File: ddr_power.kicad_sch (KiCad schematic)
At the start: 27 parts, among them U2 MT53D512M32D2DS

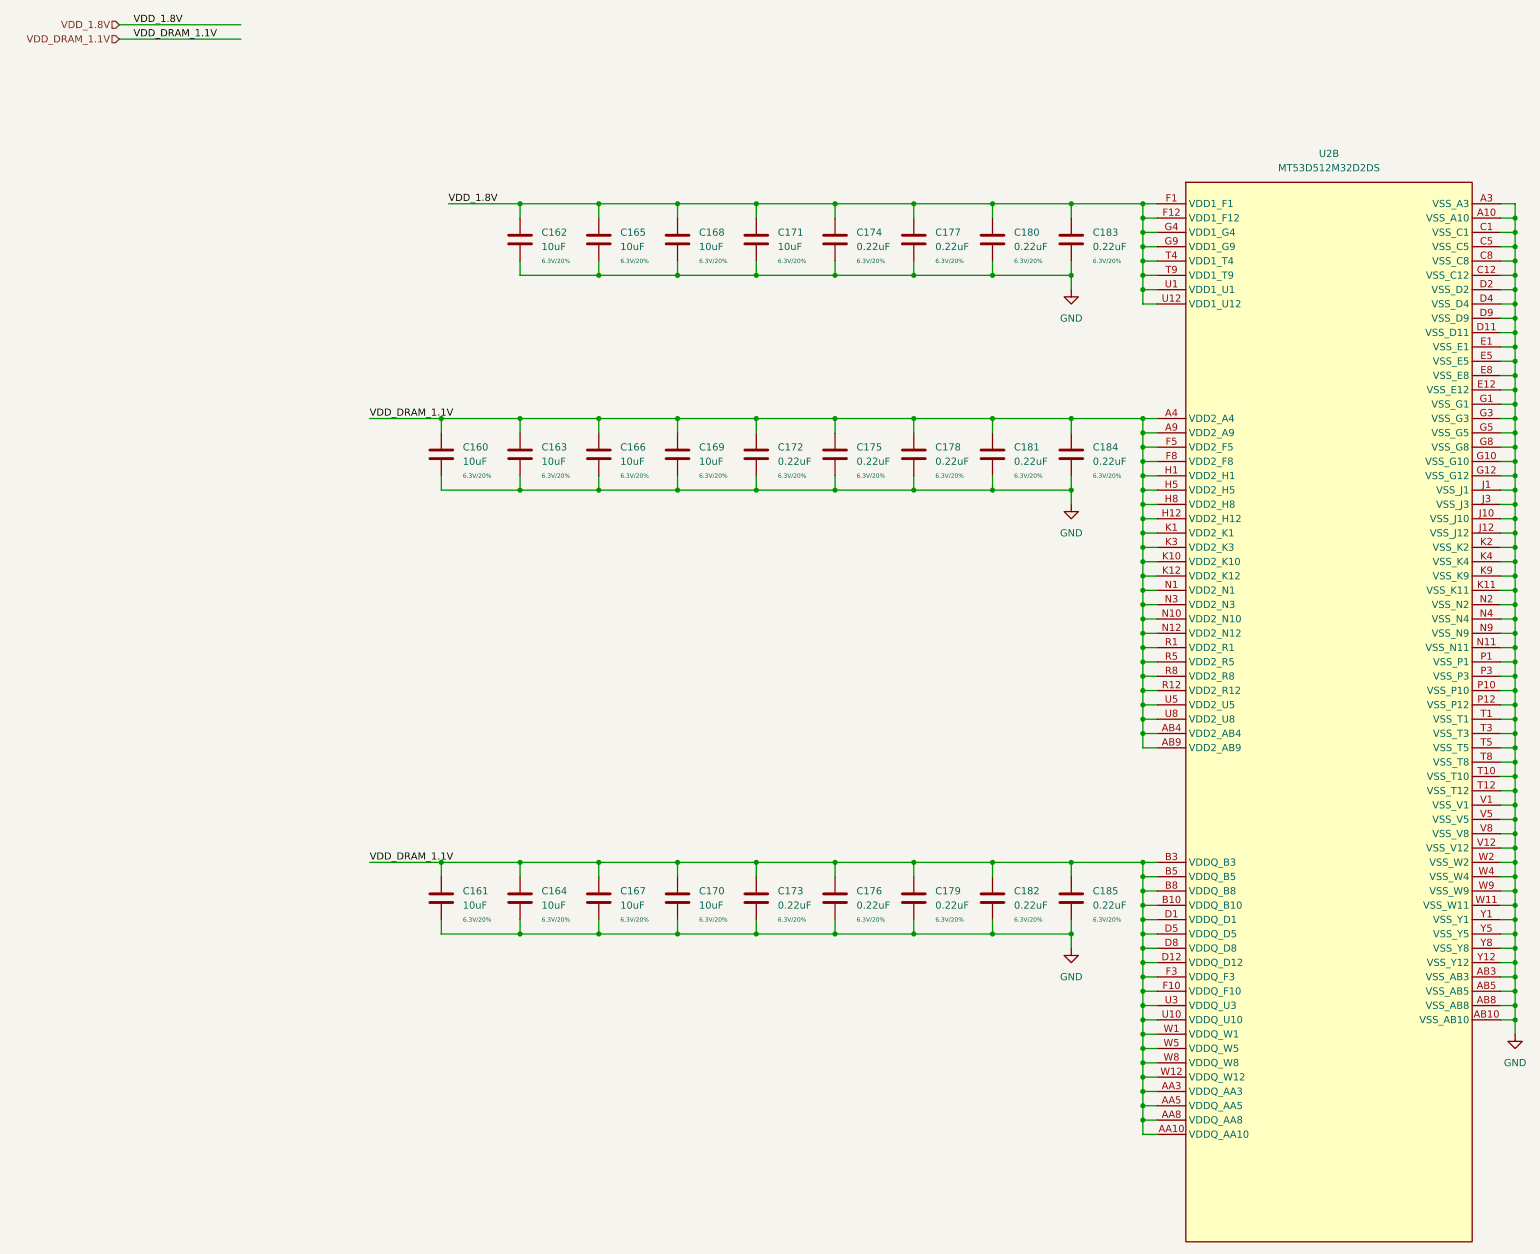
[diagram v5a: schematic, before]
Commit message: misc cleanup, change from usb mux to dual uart
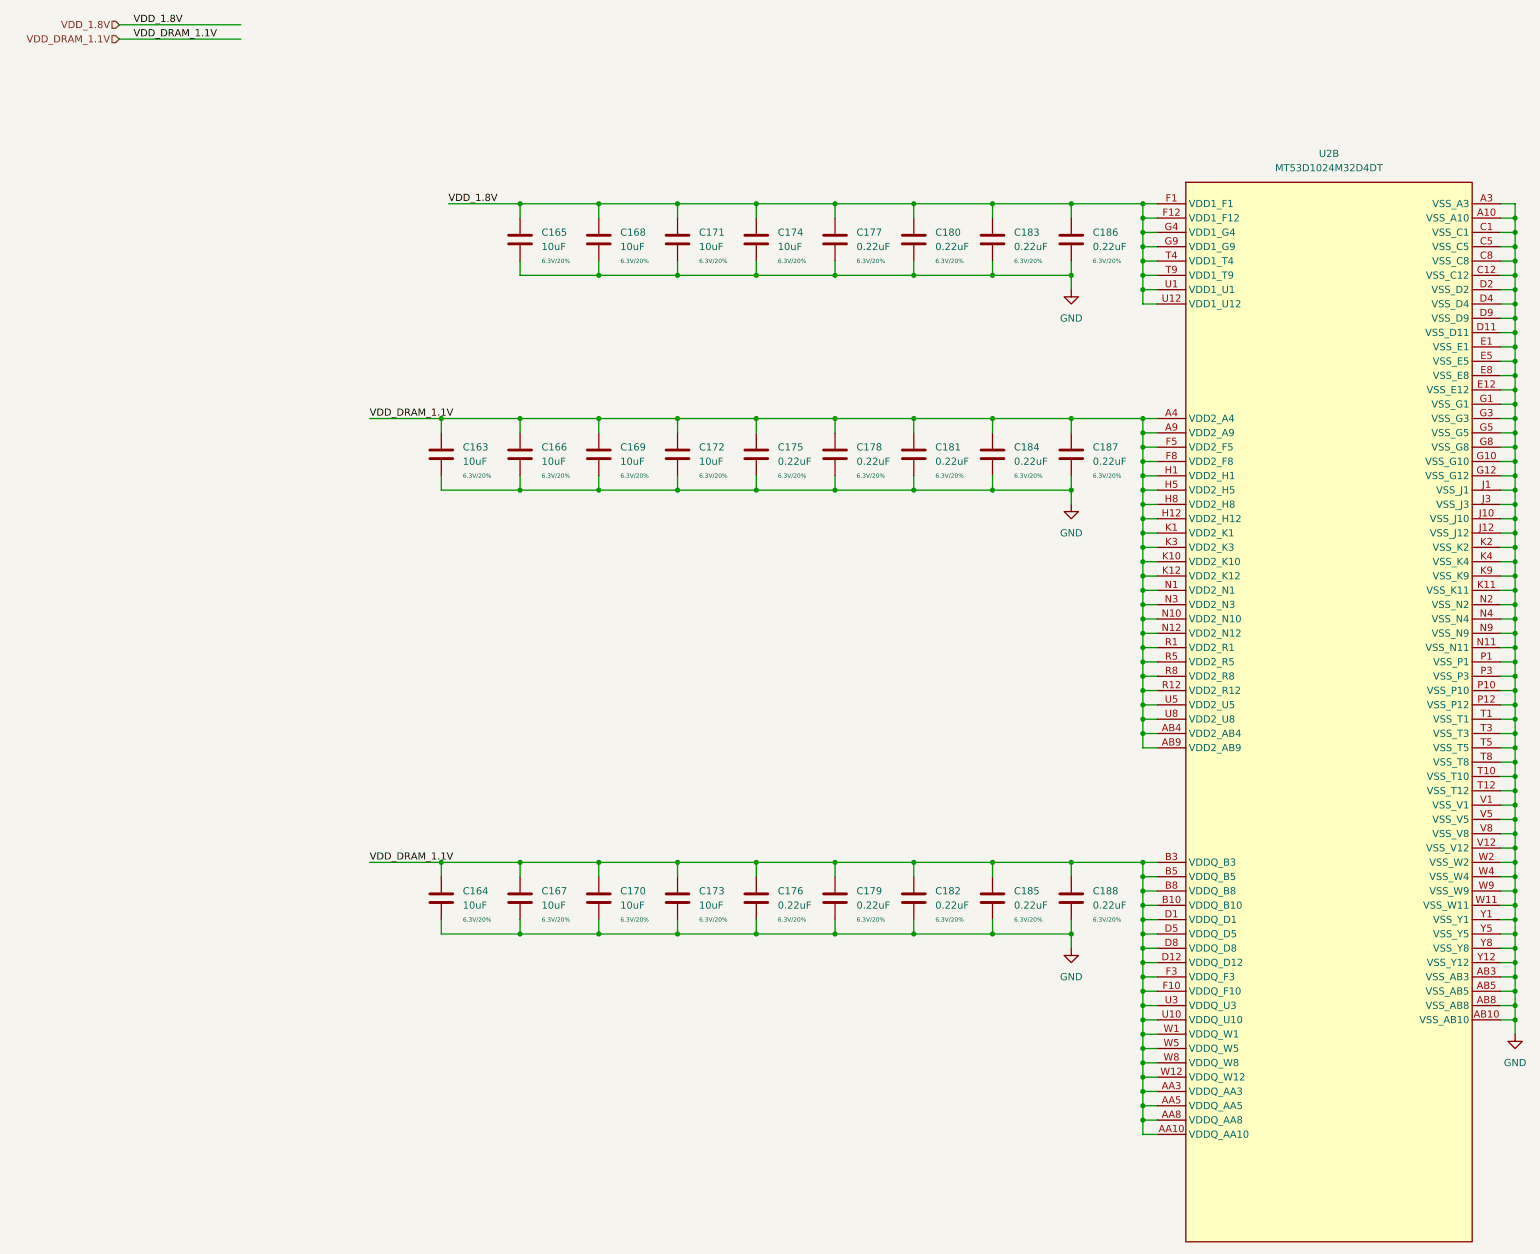
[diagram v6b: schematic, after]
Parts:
- U2: value MT53D512M32D2DS -> MT53D1024M32D4DT
- renumbered C160 to C163, C161 to C164, C162 to C165, C163 to C166, C164 to C167, C165 to C168, C166 to C169, C167 to C170, C168 to C171, C169 to C172, C170 to C173, C171 to C174, C172 to C175, C173 to C176, C174 to C177, C175 to C178, C176 to C179, C177 to C180, C178 to C181, C179 to C182, C180 to C183, C181 to C184, C182 to C185, C183 to C186, C184 to C187, C185 to C188
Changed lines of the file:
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@@
   (symbol (lib_id "Device:C") (at 120.65 59.69 0) (unit 1)
     (in_bom yes) (on_board yes)
-    (property "Reference" "C165" (id 0) (at 124.46 58.4199 0)
+    (property "Reference" "C168" (id 0) (at 124.46 58.4199 0)
       (effects (font (size 1.27 1.27)) (justify left))
     )
@@
   (symbol (lib_id "Device:C") (at 190.5 59.69 0) (unit 1)
     (in_bom yes) (on_board yes)
-    (property "Reference" "C180" (id 0) (at 194.31 58.4199 0)
+    (property "Reference" "C183" (id 0) (at 194.31 58.4199 0)
       (effects (font (size 1.27 1.27)) (justify left))
     )
@@
   (symbol (lib_id "Device:C") (at 162.56 97.79 0) (unit 1)
     (in_bom yes) (on_board yes)
-    (property "Reference" "C175" (id 0) (at 166.37 96.5199 0)
+    (property "Reference" "C178" (id 0) (at 166.37 96.5199 0)
       (effects (font (size 1.27 1.27)) (justify left))
     )
@@
   (symbol (lib_id "Device:C") (at 190.5 176.53 0) (unit 1)
     (in_bom yes) (on_board yes)
-    (property "Reference" "C182" (id 0) (at 194.31 175.2599 0)
+    (property "Reference" "C185" (id 0) (at 194.31 175.2599 0)
       (effects (font (size 1.27 1.27)) (justify left))
     )
@@
     (in_bom yes) (on_board yes) (fields_autoplaced)
     (property "Reference" "U2" (id 0) (at 250.19 44.45 0))
-    (property "Value" "MT53D512M32D2DS" (id 1) (at 250.19 46.99 0))
+    (property "Value" "MT53D1024M32D4DT" (id 1) (at 250.19 46.99 0))
     (property "Footprint" "Package_BGA:BGA-200_10.0x14.5mm_Layout12x22_P0.80x0.65mm" (id 2) (at 250.19 243.84 0)
       (effects (font (size 1.27 1.27)) hide)
@@
   (symbol (lib_id "Device:C") (at 148.59 59.69 0) (unit 1)
     (in_bom yes) (on_board yes)
-    (property "Reference" "C171" (id 0) (at 152.4 58.4199 0)
+    (property "Reference" "C174" (id 0) (at 152.4 58.4199 0)
       (effects (font (size 1.27 1.27)) (justify left))
     )
@@
   (symbol (lib_id "Device:C") (at 190.5 97.79 0) (unit 1)
     (in_bom yes) (on_board yes)
-    (property "Reference" "C181" (id 0) (at 194.31 96.5199 0)
+    (property "Reference" "C184" (id 0) (at 194.31 96.5199 0)
       (effects (font (size 1.27 1.27)) (justify left))
     )
@@
   (symbol (lib_id "Device:C") (at 176.53 59.69 0) (unit 1)
     (in_bom yes) (on_board yes)
-    (property "Reference" "C177" (id 0) (at 180.34 58.4199 0)
+    (property "Reference" "C180" (id 0) (at 180.34 58.4199 0)
       (effects (font (size 1.27 1.27)) (justify left))
     )
@@
   (symbol (lib_id "power:GND") (at 204.47 68.58 0) (unit 1)
     (in_bom yes) (on_board yes) (fields_autoplaced)
-    (property "Reference" "#PWR0156" (id 0) (at 204.47 74.93 0)
+    (property "Reference" "#PWR0160" (id 0) (at 204.47 74.93 0)
       (effects (font (size 1.27 1.27)) hide)
     )
@@
   (symbol (lib_id "Device:C") (at 134.62 59.69 0) (unit 1)
     (in_bom yes) (on_board yes)
-    (property "Reference" "C168" (id 0) (at 138.43 58.4199 0)
+    (property "Reference" "C171" (id 0) (at 138.43 58.4199 0)
       (effects (font (size 1.27 1.27)) (justify left))
     )
@@
   (symbol (lib_id "Device:C") (at 204.47 176.53 0) (unit 1)
     (in_bom yes) (on_board yes)
-    (property "Reference" "C185" (id 0) (at 208.28 175.2599 0)
+    (property "Reference" "C188" (id 0) (at 208.28 175.2599 0)
       (effects (font (size 1.27 1.27)) (justify left))
     )
@@
   (symbol (lib_id "Device:C") (at 92.71 176.53 0) (unit 1)
     (in_bom yes) (on_board yes)
-    (property "Reference" "C161" (id 0) (at 96.52 175.2599 0)
+    (property "Reference" "C164" (id 0) (at 96.52 175.2599 0)
       (effects (font (size 1.27 1.27)) (justify left))
     )
@@
   (symbol (lib_id "Device:C") (at 204.47 97.79 0) (unit 1)
     (in_bom yes) (on_board yes)
-    (property "Reference" "C184" (id 0) (at 208.28 96.5199 0)
+    (property "Reference" "C187" (id 0) (at 208.28 96.5199 0)
       (effects (font (size 1.27 1.27)) (justify left))
     )
@@
   (symbol (lib_id "Device:C") (at 204.47 59.69 0) (unit 1)
     (in_bom yes) (on_board yes)
-    (property "Reference" "C183" (id 0) (at 208.28 58.4199 0)
+    (property "Reference" "C186" (id 0) (at 208.28 58.4199 0)
       (effects (font (size 1.27 1.27)) (justify left))
     )
@@
   (symbol (lib_id "Device:C") (at 120.65 97.79 0) (unit 1)
     (in_bom yes) (on_board yes)
-    (property "Reference" "C166" (id 0) (at 124.46 96.5199 0)
+    (property "Reference" "C169" (id 0) (at 124.46 96.5199 0)
       (effects (font (size 1.27 1.27)) (justify left))
     )
@@
   (symbol (lib_id "Device:C") (at 176.53 176.53 0) (unit 1)
     (in_bom yes) (on_board yes)
-    (property "Reference" "C179" (id 0) (at 180.34 175.2599 0)
+    (property "Reference" "C182" (id 0) (at 180.34 175.2599 0)
       (effects (font (size 1.27 1.27)) (justify left))
     )
@@
   (symbol (lib_id "power:GND") (at 204.47 106.68 0) (unit 1)
     (in_bom yes) (on_board yes) (fields_autoplaced)
-    (property "Reference" "#PWR0157" (id 0) (at 204.47 113.03 0)
+    (property "Reference" "#PWR0161" (id 0) (at 204.47 113.03 0)
       (effects (font (size 1.27 1.27)) hide)
     )
@@
   (symbol (lib_id "power:GND") (at 204.47 185.42 0) (unit 1)
     (in_bom yes) (on_board yes) (fields_autoplaced)
-    (property "Reference" "#PWR0158" (id 0) (at 204.47 191.77 0)
+    (property "Reference" "#PWR0162" (id 0) (at 204.47 191.77 0)
       (effects (font (size 1.27 1.27)) hide)
     )
@@
   (symbol (lib_id "Device:C") (at 162.56 59.69 0) (unit 1)
     (in_bom yes) (on_board yes)
-    (property "Reference" "C174" (id 0) (at 166.37 58.4199 0)
+    (property "Reference" "C177" (id 0) (at 166.37 58.4199 0)
       (effects (font (size 1.27 1.27)) (justify left))
     )
@@
   (symbol (lib_id "Device:C") (at 148.59 97.79 0) (unit 1)
     (in_bom yes) (on_board yes)
-    (property "Reference" "C172" (id 0) (at 152.4 96.5199 0)
+    (property "Reference" "C175" (id 0) (at 152.4 96.5199 0)
       (effects (font (size 1.27 1.27)) (justify left))
     )
@@
   (symbol (lib_id "Device:C") (at 106.68 59.69 0) (unit 1)
     (in_bom yes) (on_board yes)
-    (property "Reference" "C162" (id 0) (at 110.49 58.4199 0)
+    (property "Reference" "C165" (id 0) (at 110.49 58.4199 0)
       (effects (font (size 1.27 1.27)) (justify left))
     )
@@
   (symbol (lib_id "power:GND") (at 283.21 200.66 0) (unit 1)
     (in_bom yes) (on_board yes) (fields_autoplaced)
-    (property "Reference" "#PWR0159" (id 0) (at 283.21 207.01 0)
+    (property "Reference" "#PWR0163" (id 0) (at 283.21 207.01 0)
       (effects (font (size 1.27 1.27)) hide)
     )
@@
   (symbol (lib_id "Device:C") (at 106.68 176.53 0) (unit 1)
     (in_bom yes) (on_board yes)
-    (property "Reference" "C164" (id 0) (at 110.49 175.2599 0)
+    (property "Reference" "C167" (id 0) (at 110.49 175.2599 0)
       (effects (font (size 1.27 1.27)) (justify left))
     )
@@
   (symbol (lib_id "Device:C") (at 134.62 176.53 0) (unit 1)
     (in_bom yes) (on_board yes)
-    (property "Reference" "C170" (id 0) (at 138.43 175.2599 0)
+    (property "Reference" "C173" (id 0) (at 138.43 175.2599 0)
       (effects (font (size 1.27 1.27)) (justify left))
     )
@@
   (symbol (lib_id "Device:C") (at 148.59 176.53 0) (unit 1)
     (in_bom yes) (on_board yes)
-    (property "Reference" "C173" (id 0) (at 152.4 175.2599 0)
+    (property "Reference" "C176" (id 0) (at 152.4 175.2599 0)
       (effects (font (size 1.27 1.27)) (justify left))
     )
@@
   (symbol (lib_id "Device:C") (at 134.62 97.79 0) (unit 1)
     (in_bom yes) (on_board yes)
-    (property "Reference" "C169" (id 0) (at 138.43 96.5199 0)
+    (property "Reference" "C172" (id 0) (at 138.43 96.5199 0)
       (effects (font (size 1.27 1.27)) (justify left))
     )
@@
   (symbol (lib_id "Device:C") (at 106.68 97.79 0) (unit 1)
     (in_bom yes) (on_board yes)
-    (property "Reference" "C163" (id 0) (at 110.49 96.5199 0)
+    (property "Reference" "C166" (id 0) (at 110.49 96.5199 0)
       (effects (font (size 1.27 1.27)) (justify left))
     )
@@
   (symbol (lib_id "Device:C") (at 162.56 176.53 0) (unit 1)
     (in_bom yes) (on_board yes)
-    (property "Reference" "C176" (id 0) (at 166.37 175.2599 0)
+    (property "Reference" "C179" (id 0) (at 166.37 175.2599 0)
       (effects (font (size 1.27 1.27)) (justify left))
     )
@@
   (symbol (lib_id "Device:C") (at 120.65 176.53 0) (unit 1)
     (in_bom yes) (on_board yes)
-    (property "Reference" "C167" (id 0) (at 124.46 175.2599 0)
+    (property "Reference" "C170" (id 0) (at 124.46 175.2599 0)
       (effects (font (size 1.27 1.27)) (justify left))
     )
@@
   (symbol (lib_id "Device:C") (at 176.53 97.79 0) (unit 1)
     (in_bom yes) (on_board yes)
-    (property "Reference" "C178" (id 0) (at 180.34 96.5199 0)
+    (property "Reference" "C181" (id 0) (at 180.34 96.5199 0)
       (effects (font (size 1.27 1.27)) (justify left))
     )
@@
   (symbol (lib_id "Device:C") (at 92.71 97.79 0) (unit 1)
     (in_bom yes) (on_board yes)
-    (property "Reference" "C160" (id 0) (at 96.52 96.5199 0)
-      (effects (font (size 1.27 1.27)) (justify left))
-    )
+    (property "Reference" "C163" (id 0) (at 96.52 96.5199 0)
+      (effects (font (size 1.27 1.27)) (justify left))
+    )

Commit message: add imx8mm 3d model, add FIDs
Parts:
- U2: MPN MT53D512M32D2DS-053WT:D -> MT53D1024M32D4DT-046 WT:D
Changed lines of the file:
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@@
       (effects (font (size 1.27 1.27)) hide)
     )
-    (property "MPN" "MT53D512M32D2DS-053WT:D" (id 4) (at 250.19 125.73 0)
+    (property "MPN" "MT53D1024M32D4DT-046 WT:D" (id 4) (at 250.19 125.73 0)
       (effects (font (size 1.27 1.27)) hide)
     )

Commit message: Rev 1
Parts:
- U2: footprint Package_BGA:BGA-200_10.0x14.5mm_Layout12x22_P0.80x0.65mm -> qsbc:BGA-200_10.0x14.5mm_Layout12x22_P0.80x0.65mm
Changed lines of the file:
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@@
   (title_block
     (title "QSBC")
-    (rev "1")
+    (date "2022-12-01")
+    (rev "1.0")
     (company "Q-LAB")
   )
@@
     (property "Reference" "U2" (id 0) (at 250.19 44.45 0))
     (property "Value" "MT53D1024M32D4DT" (id 1) (at 250.19 46.99 0))
-    (property "Footprint" "Package_BGA:BGA-200_10.0x14.5mm_Layout12x22_P0.80x0.65mm" (id 2) (at 250.19 243.84 0)
+    (property "Footprint" "qsbc:BGA-200_10.0x14.5mm_Layout12x22_P0.80x0.65mm" (id 2) (at 250.19 243.84 0)
       (effects (font (size 1.27 1.27)) hide)
     )
@@
   (symbol (lib_id "power:GND") (at 204.47 68.58 0) (unit 1)
     (in_bom yes) (on_board yes) (fields_autoplaced)
-    (property "Reference" "#PWR0160" (id 0) (at 204.47 74.93 0)
+    (property "Reference" "#PWR0159" (id 0) (at 204.47 74.93 0)
       (effects (font (size 1.27 1.27)) hide)
     )
@@
   (symbol (lib_id "power:GND") (at 204.47 106.68 0) (unit 1)
     (in_bom yes) (on_board yes) (fields_autoplaced)
-    (property "Reference" "#PWR0161" (id 0) (at 204.47 113.03 0)
+    (property "Reference" "#PWR0160" (id 0) (at 204.47 113.03 0)
       (effects (font (size 1.27 1.27)) hide)
     )
@@
   (symbol (lib_id "power:GND") (at 204.47 185.42 0) (unit 1)
     (in_bom yes) (on_board yes) (fields_autoplaced)
-    (property "Reference" "#PWR0162" (id 0) (at 204.47 191.77 0)
+    (property "Reference" "#PWR0161" (id 0) (at 204.47 191.77 0)
       (effects (font (size 1.27 1.27)) hide)
     )
@@
   (symbol (lib_id "power:GND") (at 283.21 200.66 0) (unit 1)
     (in_bom yes) (on_board yes) (fields_autoplaced)
-    (property "Reference" "#PWR0163" (id 0) (at 283.21 207.01 0)
-      (effects (font (size 1.27 1.27)) hide)
-    )
+    (property "Reference" "#PWR0162" (id 0) (at 283.21 207.01 0)
+      (effects (font (size 1.27 1.27)) hide)
+    )
